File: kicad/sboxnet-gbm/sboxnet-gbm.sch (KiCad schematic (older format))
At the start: 42 parts, among them J1 Screw_Terminal_01x04, J2 Screw_Terminal_01x04, J3 Screw_Terminal_01x04, J4 sboxnet-stecker_02x17, J5 Screw_Terminal_01x04, U1 LTV-844, U2 LTV-844, U3 LTV-844, U4 SN65HVD230

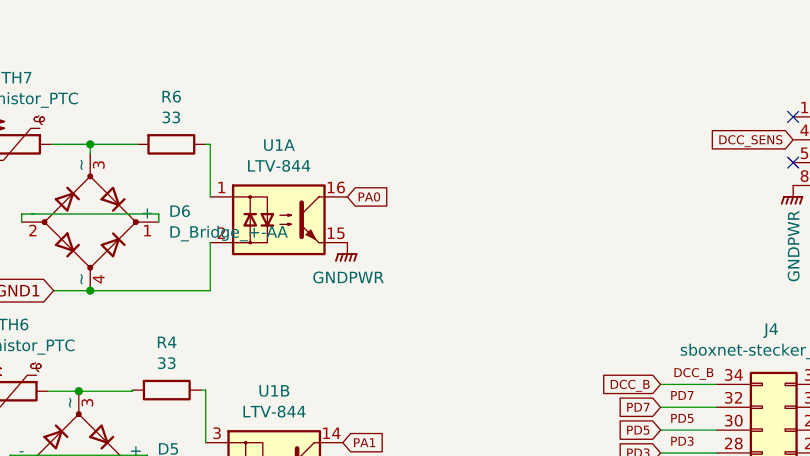
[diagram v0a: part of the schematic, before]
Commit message: booster DCC Input
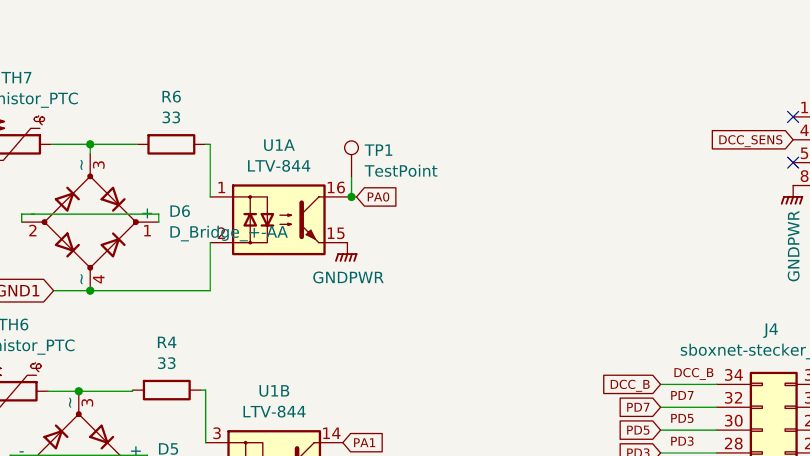
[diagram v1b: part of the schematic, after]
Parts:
- added TP1: TestPoint, Connector_PinHeader_2.54mm:PinHeader_1x01_P2.54mm_Vertical, symbol Connector:TestPoint
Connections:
- net PA0: now also TP1.1
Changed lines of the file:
@@
 	1    0    0    -1
 $EndComp
-Text GLabel 2960 1825 2    39   Input ~ 0
+Text GLabel 3000 1825 2    39   Input ~ 0
 PA0
 $Comp
@@
 Wire Wire Line
 	5550 3545 5550 3540
+$Comp
+L Connector:TestPoint TP1
+U 1 1 5F20F35B
+P 2978 1740
+F 0 "TP1" H 3036 1858 50  0000 L CNN
+F 1 "TestPoint" H 3036 1767 50  0000 L CNN
+F 2 "Connector_PinHeader_2.54mm:PinHeader_1x01_P2.54mm_Vertical" H 3178 1740 50  0001 C CNN
+F 3 "~" H 3178 1740 50  0001 C CNN
+	1    2978 1740
+	1    0    0    -1
+$EndComp
+Wire Wire Line
+	2960 1825 2978 1825
+Wire Wire Line
+	2978 1740 2978 1825
+Connection ~ 2978 1825
+Wire Wire Line
+	2978 1825 3000 1825
 $EndSCHEMATC
